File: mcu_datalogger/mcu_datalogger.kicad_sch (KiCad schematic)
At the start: 0 parts

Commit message: symbols and libraries for mcu
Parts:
- added BT1: Battery, symbol Device:Battery
- added C1, C2, C3, C4: C, symbol Device:C
- added C5: C_Polarized, symbol Device:C_Polarized
- added D1, D2: LED, PCM_SparkFun-LED:LED_0603_1608Metric, symbol PCM_SparkFun-LED:LED
- added H1, H2, H3, H4: MountingHole, symbol Mechanical:MountingHole
- added R1, R2, R3, R4, R5, R6, R7: R, symbol Device:R
- added U1, U2: 24LC1025, symbol Memory_EEPROM:24LC1025
- added U3: DS1337S_, DS1337S_:SOIC127P600X175-8N, symbol DS1337S_:DS1337S_
- added U4: ATMEGA328P-AU, ATMEGA328P-AU:QFP80P900X900X120-32N, symbol ATMEGA328P-AU:ATMEGA328P-AU
- added Y1, Y2: Crystal, symbol Device:Crystal
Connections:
- new net GND: U4.21 (GND), U4.3 (GND), U4.5 (GND)
- new net VCC: U4.4 (VCC), U4.6 (VCC)
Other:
- added sheet connectors (untitled.kicad_sch)
- company: (none) -> JPIndustries
- title: (none) -> ${project_name}

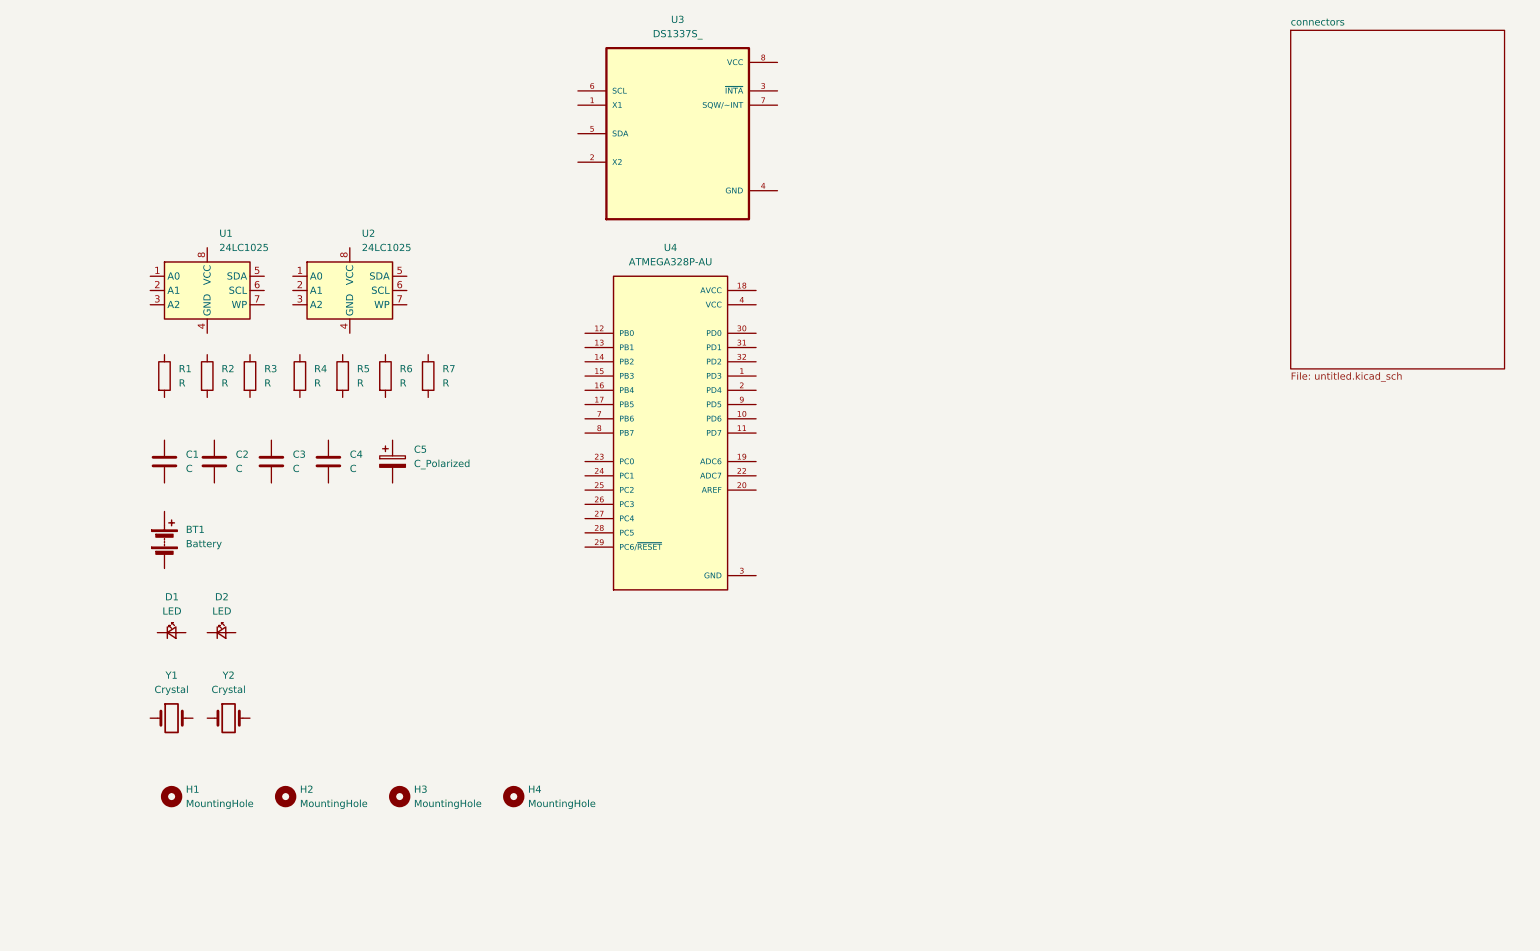
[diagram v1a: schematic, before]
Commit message: added values to symbols
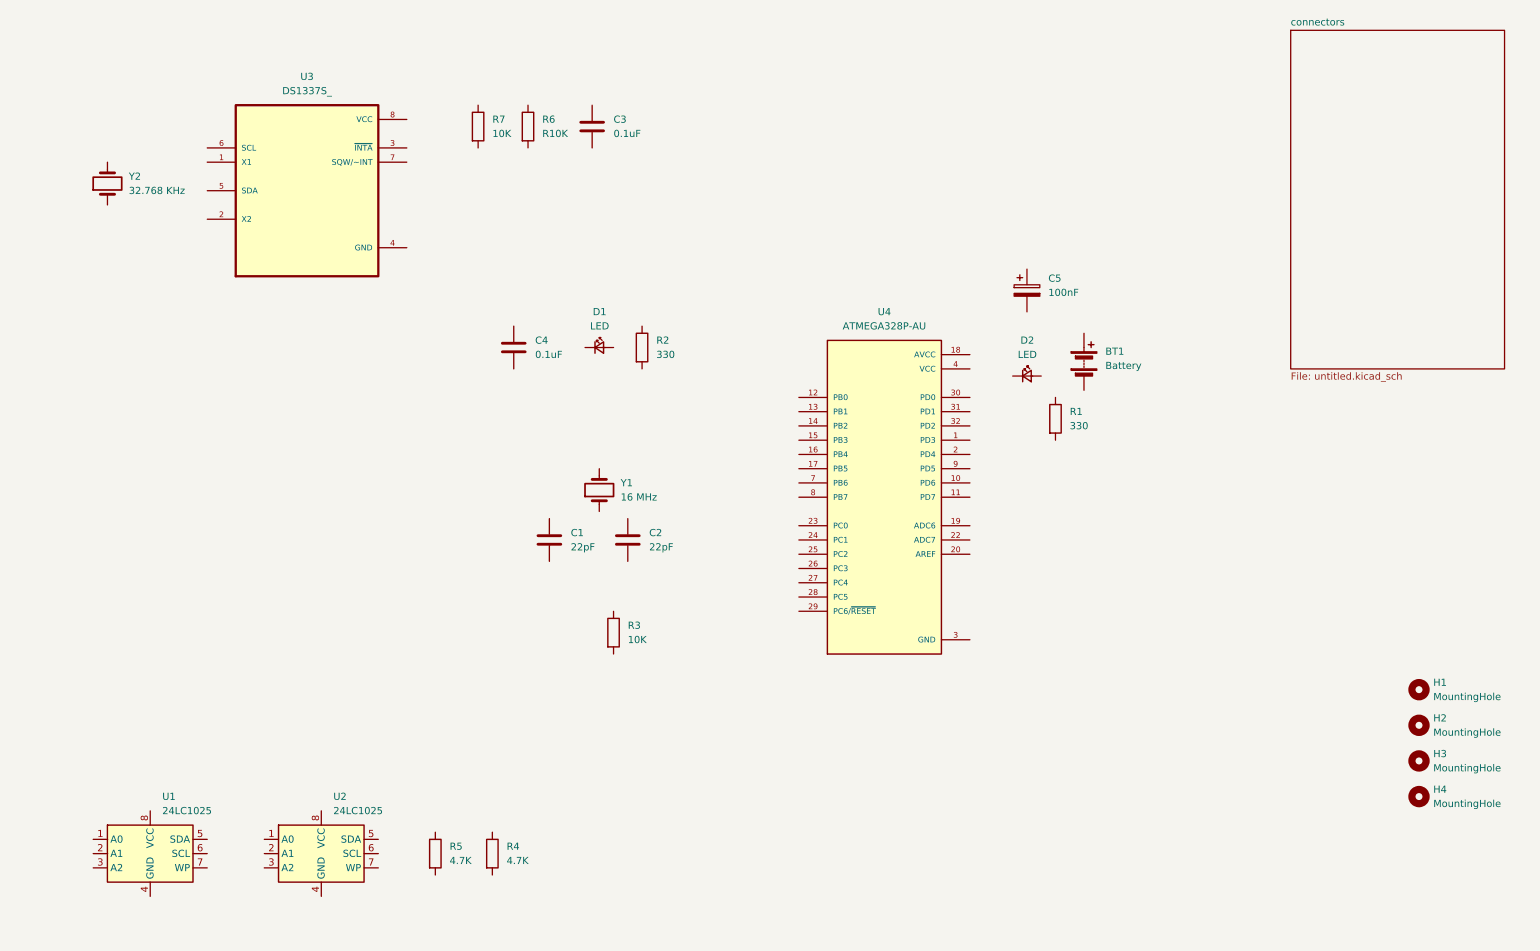
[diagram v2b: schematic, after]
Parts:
- C1, C2: value C -> 22pF
- C3, C4: value C -> 0.1uF
- C5: value C_Polarized -> 100nF
- R1, R2: value R -> 330
- R3, R7: value R -> 10K
- R4, R5: value R -> 4.7K
- R6: value R -> R10K
- Y1: value Crystal -> 16 MHz
- Y2: value Crystal -> 32.768 KHz
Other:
- moved on the sheet: BT1, C1, C2, C3, C4, C5, D1, D2, H1, H2, H3, H4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

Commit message: footprints
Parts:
- BT1: footprint (none) -> Connector_PinHeader_2.54mm:PinHeader_1x02_P2.54mm_Vertical
- C1, C2, C3, C4, C5: footprint (none) -> Capacitor_SMD:C_0805_2012Metric
- D1, D2: footprint PCM_SparkFun-LED:LED_0603_1608Metric -> LED_SMD:LED_0805_2012Metric
- H1, H2, H3, H4: footprint (none) -> MountingHole:MountingHole_2.1mm
- R1, R2, R3, R4, R5, R6, R7: footprint (none) -> Resistor_SMD:R_0805_2012Metric
- U1, U2: footprint (none) -> Package_SO:SOIC-8_5.3x5.3mm_P1.27mm
- Y1, Y2: footprint (none) -> Crystal:Crystal_SMD_5032-2Pin_5.0x3.2mm
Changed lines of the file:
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@@
 			)
 		)
-		(property "Footprint" ""
+		(property "Footprint" "MountingHole:MountingHole_2.1mm"
 			(at 265.43 153.67 0)
 			(effects
@@
 			)
 		)
-		(property "Footprint" ""
+		(property "Footprint" "Resistor_SMD:R_0805_2012Metric"
 			(at 198.882 86.36 90)
 			(effects
@@
 			)
 		)
-		(property "Footprint" ""
+		(property "Footprint" "Capacitor_SMD:C_0805_2012Metric"
 			(at 105.1052 77.47 0)
 			(effects
@@
 			)
 		)
-		(property "Footprint" "PCM_SparkFun-LED:LED_0603_1608Metric"
+		(property "Footprint" "LED_SMD:LED_0805_2012Metric"
 			(at 119.38 78.74 0)
 			(effects
@@
 			)
 		)
-		(property "Footprint" ""
+		(property "Footprint" "MountingHole:MountingHole_2.1mm"
 			(at 265.43 134.62 0)
 			(effects
@@
 			)
 		)
-		(property "Footprint" ""
+		(property "Footprint" "Crystal:Crystal_SMD_5032-2Pin_5.0x3.2mm"
 			(at 31.75 44.45 0)
 			(effects
@@
 			)
 		)
-		(property "Footprint" ""
+		(property "Footprint" "Crystal:Crystal_SMD_5032-2Pin_5.0x3.2mm"
 			(at 119.38 99.06 0)
 			(effects
@@
 			)
 		)
-		(property "Footprint" ""
+		(property "Footprint" "Capacitor_SMD:C_0805_2012Metric"
 			(at 125.4252 111.76 0)
 			(effects
@@
 			)
 		)
-		(property "Footprint" ""
+		(property "Footprint" "MountingHole:MountingHole_2.1mm"
 			(at 265.43 140.97 0)
 			(effects
@@
 			)
 		)
-		(property "Footprint" ""
+		(property "Footprint" "Capacitor_SMD:C_0805_2012Metric"
 			(at 119.0752 38.1 0)
 			(effects
@@
 			)
 		)
-		(property "Footprint" ""
+		(property "Footprint" "Resistor_SMD:R_0805_2012Metric"
 			(at 125.222 73.66 90)
 			(effects
@@
 			)
 		)
-		(property "Footprint" ""
+		(property "Footprint" "Resistor_SMD:R_0805_2012Metric"
 			(at 96.012 34.29 90)
 			(effects
@@
 			)
 		)
-		(property "Footprint" ""
+		(property "Footprint" "Package_SO:SOIC-8_5.3x5.3mm_P1.27mm"
 			(at 69.85 163.83 0)
 			(effects
@@
 			)
 		)
-		(property "Footprint" ""
+		(property "Footprint" "MountingHole:MountingHole_2.1mm"
 			(at 265.43 147.32 0)
 			(effects
@@
 			)
 		)
-		(property "Footprint" ""
+		(property "Footprint" "Resistor_SMD:R_0805_2012Metric"
 			(at 88.392 163.83 90)
 			(effects
@@
 			)
 		)
-		(property "Footprint" ""
+		(property "Footprint" "Package_SO:SOIC-8_5.3x5.3mm_P1.27mm"
 			(at 39.37 163.83 0)
 			(effects
@@
 			)
 		)
-		(property "Footprint" ""
+		(property "Footprint" "Capacitor_SMD:C_0805_2012Metric"
 			(at 196.5452 67.31 0)
 			(effects
@@
 			)
 		)
-		(property "Footprint" "PCM_SparkFun-LED:LED_0603_1608Metric"
+		(property "Footprint" "LED_SMD:LED_0805_2012Metric"
 			(at 195.58 83.82 0)
 			(effects
@@
 			)
 		)
-		(property "Footprint" ""
+		(property "Footprint" "Resistor_SMD:R_0805_2012Metric"
 			(at 120.142 124.46 90)
 			(effects
@@
 			)
 		)
-		(property "Footprint" ""
+		(property "Footprint" "Resistor_SMD:R_0805_2012Metric"
 			(at 98.552 163.83 90)
 			(effects
@@
 			)
 		)
-		(property "Footprint" ""
+		(property "Footprint" "Capacitor_SMD:C_0805_2012Metric"
 			(at 111.4552 111.76 0)
 			(effects
@@
 			)
 		)
-		(property "Footprint" ""
+		(property "Footprint" "Resistor_SMD:R_0805_2012Metric"
 			(at 104.902 34.29 90)
 			(effects
@@
 			)
 		)
-		(property "Footprint" ""
+		(property "Footprint" "Connector_PinHeader_2.54mm:PinHeader_1x02_P2.54mm_Vertical"
 			(at 205.74 74.676 90)
 			(effects

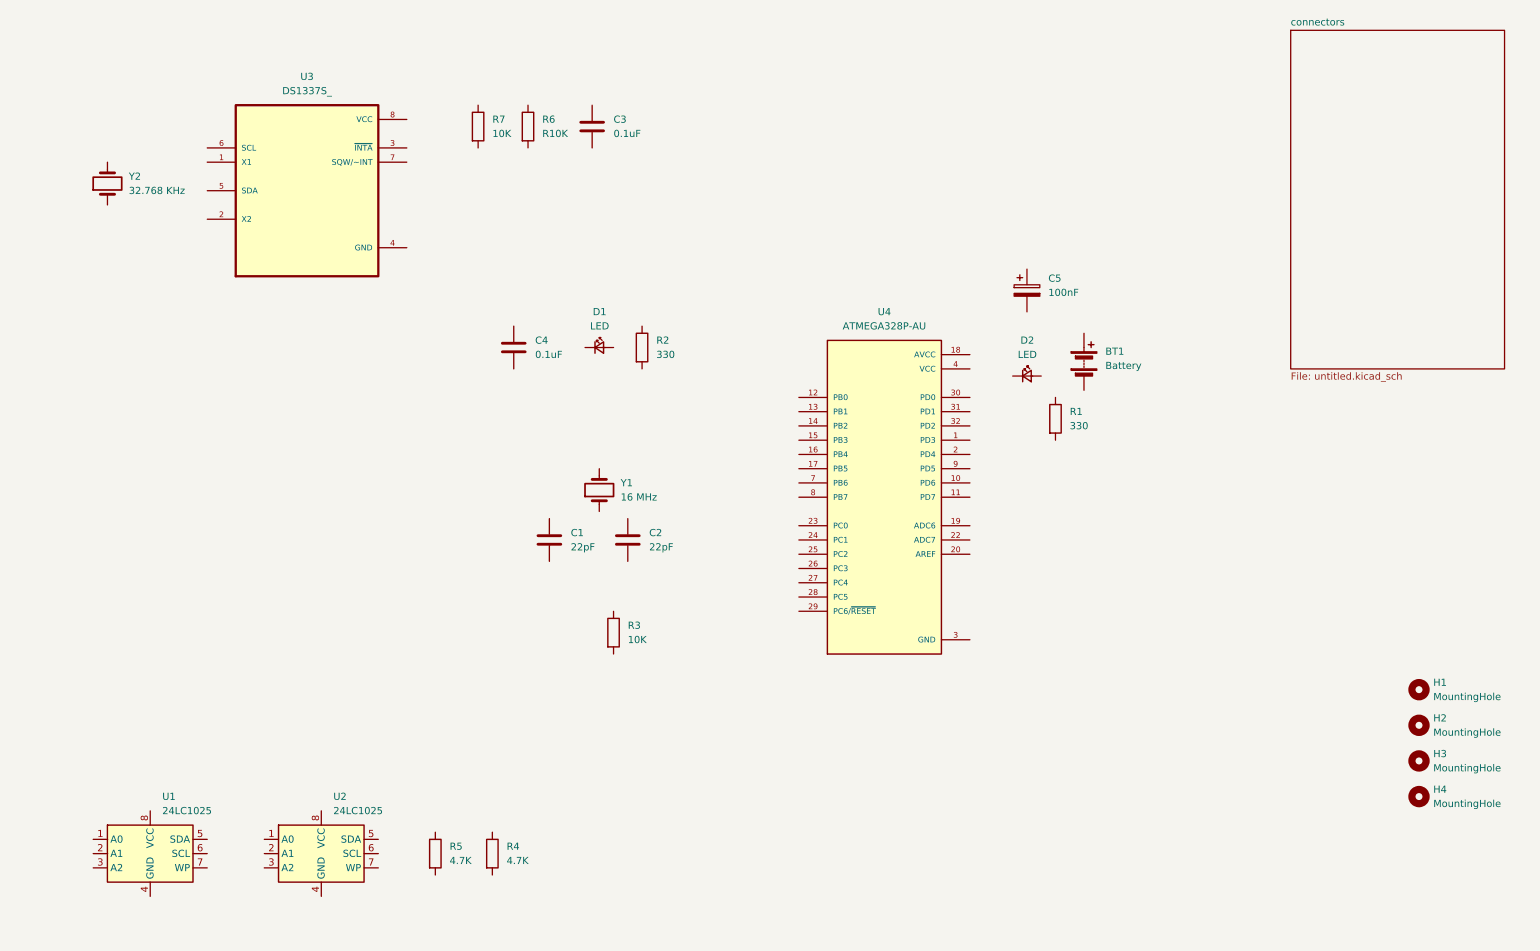
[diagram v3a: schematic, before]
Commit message: connect labels between sheets
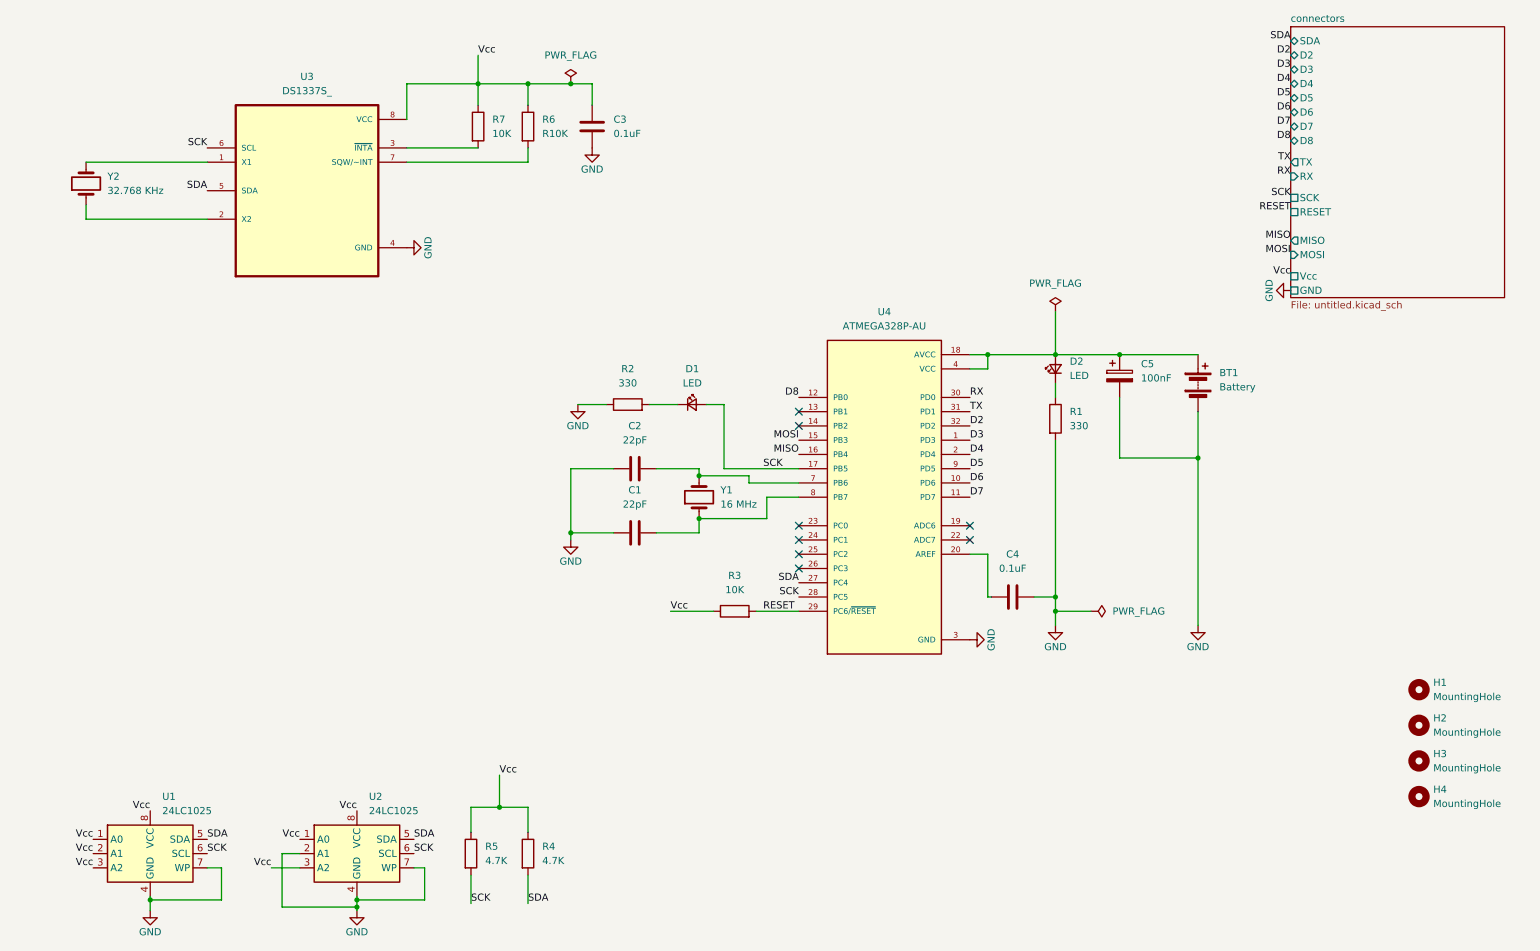
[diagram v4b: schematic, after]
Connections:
- net GND: now also BT1.2 (-), C1.1, C2.1, C3.2, C4.2, C5.2, R1.2, R2.1, U1.4 (GND), U1.7 (WP), U2.2 (A1), U2.4 (GND), U2.7 (WP), U3.4 (GND)
- net VCC: now also BT1.1 (+), C5.1, D2.2 (A), U4.18 (AVCC)
- net at R1.1: now also D2.1 (K)
- net at C4.1: now also U4.20 (AREF)
- net at D1.1 (K): now also R2.2
- net SCK: now reaches D1.2 (A)
- net SCK: now also R5.2, U1.6 (SCL), U2.6 (SCL), U3.6 (SCL), U4.17 (PB5), U4.28 (PC5)
- net at Y2.1: now also U3.2 (X2)
- net at Y2.2: now also U3.1 (X1)
- net at Y1.1: now also C1.2, U4.8 (PB7)
- net at Y1.2: now also C2.2, U4.7 (PB6)
- net Vcc: now reaches C3.1
- net Vcc: now also R3.1, R4.1, R5.1, R6.1, R7.1, U1.1 (A0), U1.2 (A1), U1.3 (A2), U1.8 (VCC), U2.1 (A0), U2.3 (A2), U2.8 (VCC), U3.8 (VCC)
- net at R7.2: now also U3.3 (~{INTA})
- net SDA: now reaches U2.5 (SDA)
- net SDA: now also R4.2, U1.5 (SDA), U3.5 (SDA), U4.27 (PC4)
- net at U3.7 (SQW/~INT): now also R6.2
- net RESET: now reaches R3.2
- net RESET: now also U4.29 (PC6/~{RESET})
- net D3: now reaches U4.1 (PD3)
- net D6: now reaches U4.10 (PD6)
- net D7: now reaches U4.11 (PD7)
- net D8: now reaches U4.12 (PB0)
- net MOSI: now reaches U4.15 (PB3)
- net MISO: now reaches U4.16 (PB4)
- net D4: now reaches U4.2 (PD4)
- net RX: now reaches U4.30 (PD0)
- net TX: now reaches U4.31 (PD1)
- net D2: now reaches U4.32 (PD2)
- net D5: now reaches U4.9 (PD5)
- no-connect marks 0 -> 8
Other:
- sheet connectors ports: added D2, D3, D4, D5, D6, D7, D8, GND, MISO, MOSI, RESET, RX, SCK, SDA, TX, Vcc; removed none
- moved on the sheet: BT1, C1, C2, C4, C5, D1, D2, R2, R3, R4, R5, U2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

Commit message: comment schematic
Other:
- note added: "MCU"
- note added: "Memory"
- note added: "Mounting holes"
- note added: "Real time clock"
- moved on the sheet: BT1, C1, C2, C4, C5, D1, D2, R1, R2, R3, R4, R5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

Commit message: FIX PINS
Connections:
- net SCK: no longer R5.2, U1.6 (SCL), U2.6 (SCL), U3.6 (SCL), U4.28 (PC5)
- new net SCL: R5.2, U1.6 (SCL), U2.6 (SCL), U3.6 (SCL), U4.28 (PC5)
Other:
- sheet connectors ports: added SCL; removed none
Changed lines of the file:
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@@
 		)
 	)
+	(label "SCL"
+		(at 49.53 38.1 180)
+		(effects
+			(font
+				(size 1.27 1.27)
+			)
+			(justify right bottom)
+		)
+	)
+	(label "SCL"
+		(at 88.9 156.21 0)
+		(effects
+			(font
+				(size 1.27 1.27)
+			)
+			(justify left bottom)
+		)
+	)
 	(label "Vcc"
 		(at 68.58 139.7 180)
@@
 		)
 	)
-	(label "SCK"
-		(at 242.57 46.99 180)
-		(effects
-			(font
-				(size 1.27 1.27)
-			)
-			(justify right bottom)
-		)
-	)
 	(label "Vcc"
 		(at 242.57 60.96 180)
@@
 		)
 	)
-	(label "SCK"
-		(at 78.74 147.32 0)
+	(label "SCL"
+		(at 41.91 147.32 0)
 		(effects
 			(font
@@
 		)
 	)
-	(label "SCK"
+	(label "SCL"
 		(at 163.83 139.7 180)
 		(effects
@@
 		)
 	)
+	(label "SCK"
+		(at 242.57 46.99 180)
+		(effects
+			(font
+				(size 1.27 1.27)
+			)
+			(justify right bottom)
+		)
+	)
 	(label "MOSI"
 		(at 242.57 57.15 180)
@@
 		)
 	)
-	(label "D8"
-		(at 163.83 104.14 180)
+	(label "SCL"
+		(at 78.74 147.32 0)
 		(effects
 			(font
 				(size 1.27 1.27)
 			)
-			(justify right bottom)
+			(justify left bottom)
 		)
 	)
-	(label "SCK"
-		(at 49.53 38.1 180)
+	(label "SCL"
+		(at 280.67 21.59 0)
+		(effects
+			(font
+				(size 1.27 1.27)
+			)
+			(justify left bottom)
+		)
+	)
+	(label "D8"
+		(at 163.83 104.14 180)
 		(effects
 			(font
@@
 		)
 	)
-	(label "SCK"
-		(at 88.9 156.21 0)
-		(effects
-			(font
-				(size 1.27 1.27)
-			)
-			(justify left bottom)
-		)
-	)
 	(label "MOSI"
 		(at 163.83 111.76 180)
@@
 		)
 	)
-	(label "SCK"
-		(at 41.91 147.32 0)
-		(effects
-			(font
-				(size 1.27 1.27)
-			)
-			(justify left bottom)
-		)
-	)
 	(label "D6"
 		(at 194.31 119.38 0)
@@
 			)
 		)
+		(pin "SCL" bidirectional
+			(at 280.67 21.59 0)
+			(effects
+				(font
+					(size 1.27 1.27)
+				)
+				(justify right)
+			)
+		)
